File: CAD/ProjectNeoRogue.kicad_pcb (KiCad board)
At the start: 4 copper layers, 89 x 99 mm, 72 parts, among them J1 5v GND, J2 Micro_SD_Card, J3 JTAG, J4 UART, J5 Reset Jumper, J6 Boot Jumper, J8 USB_C_Plug_USB2.0, SW1 SW_SPDT, SW2 Boot, SW3 Reset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

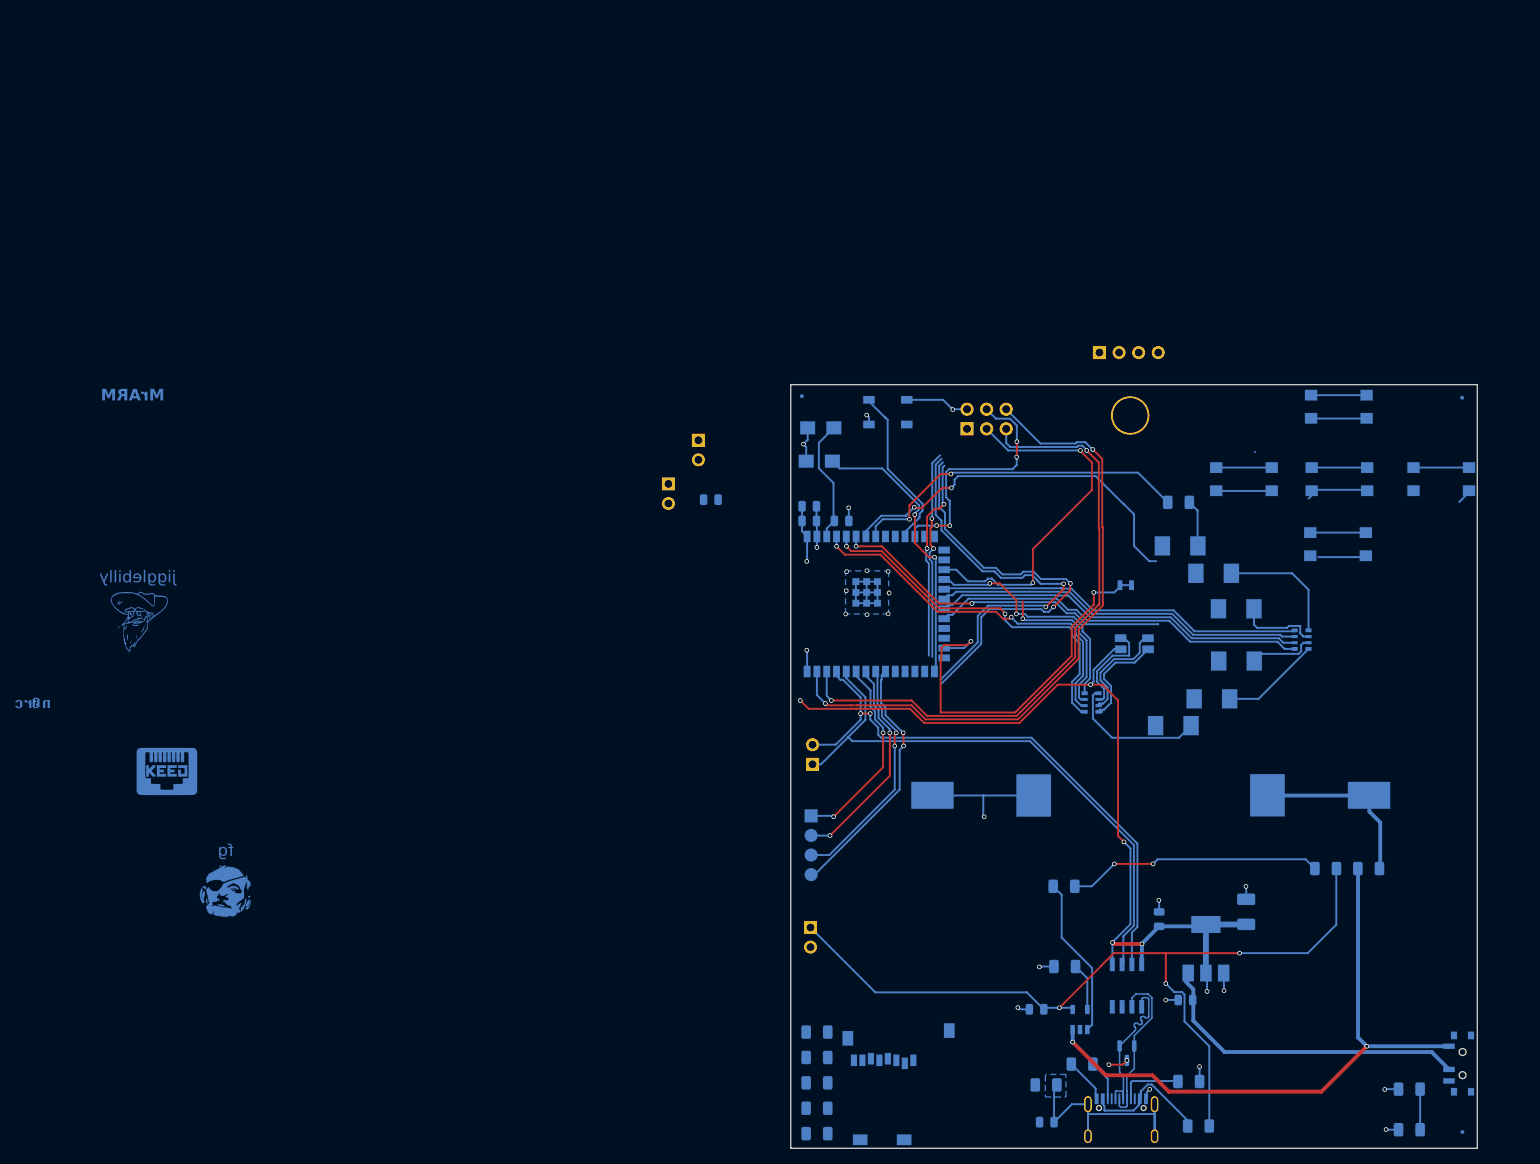
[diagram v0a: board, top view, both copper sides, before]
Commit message: adding footprints and starting to route
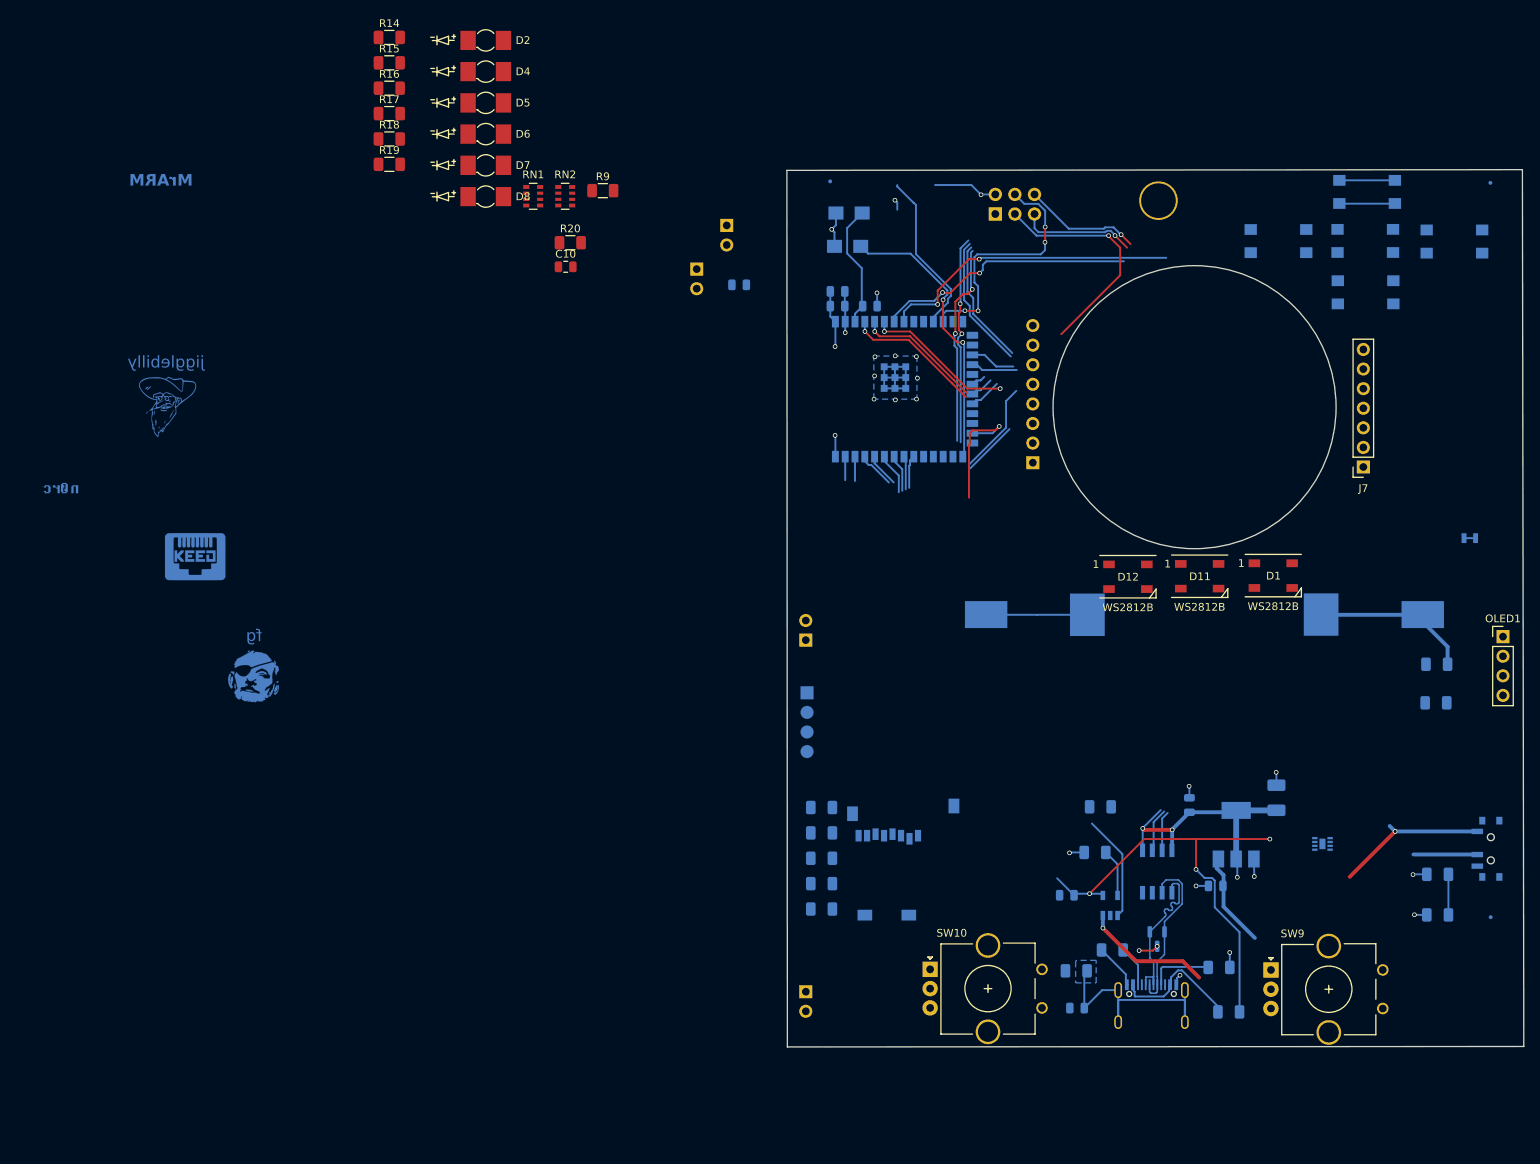
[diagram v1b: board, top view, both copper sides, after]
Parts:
- removed D3: LED, BadgePirates:LED_Osram_Lx_P47F_D2mm_ReverseMount_Proper_Mask Only
- added C10: 0.1uF, BadgePirates:C_0805_2012Metric, F.Cu at (100.4, 45.2)
- added D11: WS2812B, BadgePirates:LED_WS2812B_PLCC4_5.0x5.0mm_P3.2mm, F.Cu at (182.6, 85.3)
- added D12: WS2812B, BadgePirates:LED_WS2812B_PLCC4_5.0x5.0mm_P3.2mm, F.Cu at (173.2, 85.4)
- added J7: RoundDisplay_SPI, Connector_PinSocket_2.54mm:PinSocket_1x07_P2.54mm_Vertical, F.Cu at (203.8, 71.2)
- added J9: RoundDisplay_SPI_v2, Connector_PinSocket_2.54mm:PinSocket_1x08_P2.54mm_Vertical, B.Cu at (160.9, 70.6)
- added R14: 10k, BadgePirates:R_1206_3216Metric, F.Cu at (77.5, 15.5)
- added R15: 10k, BadgePirates:R_1206_3216Metric, F.Cu at (77.5, 18.8)
- added R16: 10k, BadgePirates:R_1206_3216Metric, F.Cu at (77.5, 22.1)
- added R17: 10k, BadgePirates:R_1206_3216Metric, F.Cu at (77.5, 25.4)
- added R18: 10k, BadgePirates:R_1206_3216Metric, F.Cu at (77.5, 28.7)
- added R19: 10k, BadgePirates:R_1206_3216Metric, F.Cu at (77.5, 31.9)
- added R20: 10K, BadgePirates:R_1206_3216Metric, F.Cu at (101.0, 42.1)
- added SW10: RotaryEncoder_Switch, Rotary_Encoder:RotaryEncoder_Alps_EC11E_Vertical_H20mm_CircularMountingHoles, F.Cu at (147.6, 136.3)
- added SW9: RotaryEncoder_Switch, Rotary_Encoder:RotaryEncoder_Alps_EC11E_Vertical_H20mm_CircularMountingHoles, F.Cu at (191.8, 136.4)
- added U5: MAX17048, BadgePirates:MAX17048_TDFN, B.Cu at (198.5, 120.0)
- D1, D4, D5, D6, D7, D8, OLED1, R9, RN1, RN2: moved to F.Cu
- D2: footprint BadgePirates:LED_RGB_1210 -> BadgePirates:LED_Osram_Lx_P47F_D2mm_ReverseMount_Proper_Mask Only; moved to F.Cu
- moved D4 124.4 mm to (90.0, 19.9)
- moved D5 121.3 mm to (90.0, 24.0)
- moved D6 115.1 mm to (90.0, 28.0)
- moved D2 114.8 mm to (90.0, 15.9)
- moved RN2 111.4 mm to (100.3, 36.1), turned to 0 degrees
- moved D7 108.2 mm to (90.0, 32.1)
- moved D8 100.8 mm to (90.0, 36.1)
- moved RN1 97.7 mm to (96.2, 36.1), turned to 0 degrees
- moved R9 84.9 mm to (105.2, 35.4)
- moved OLED1 64.0 mm to (221.9, 93.2), turned to 0 degrees
- moved D1 54.3 mm to (192.1, 85.3), turned to 0 degrees
- moved JP1 45.0 mm to (217.8, 80.4)
- moved SW7 32.8 mm to (204.1, 48.5)
- moved SW6 31.2 mm to (192.8, 41.9)
- moved SW5 31.1 mm to (204.0, 41.9)
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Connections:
- D1 pad 2: unconnected-(D1-DOUT-Pad2) -> Net-(D1-DOUT)
- D2 pad 1: Net-(D2-RK) -> GND
- D2 pad 2: VCC -> Net-(D2-A)
- RN1 pad 1: Net-(D3-A) -> Net-(D2-A)
- RN1 pad 2: Net-(D2-BK) -> unconnected-(RN1-R2.1-Pad2)
- RN1 pad 3: Net-(D2-GK) -> unconnected-(RN1-R3.1-Pad3)
- RN1 pad 4: Net-(D2-RK) -> unconnected-(RN1-R4.1-Pad4)
- RN1 pad 5: IO05 -> unconnected-(RN1-R4.2-Pad5)
- RN1 pad 6: IO04 -> unconnected-(RN1-R3.2-Pad6)
- RN1 pad 7: IO25 -> unconnected-(RN1-R2.2-Pad7)
- RN2 pad 1: Net-(D7-A) -> Net-(D4-A)
- RN2 pad 2: Net-(D6-A) -> Net-(D5-A)
- RN2 pad 3: Net-(D5-A) -> Net-(D6-A)
- RN2 pad 4: Net-(D4-A) -> Net-(D7-A)
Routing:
- net VCC: track 133.3 -> 51.6 mm, vias 9 -> 6
- net IO01: track 84.5 -> 18.6 mm, vias 2 -> 1
- net USB_TX_ESP_RX: track 75.5 -> 10.0 mm
- net USB_RX_ESP_TX: track 75.2 -> 10.00 mm, vias 2 -> 0
- net IO02: track 81.4 -> 18.2 mm, vias 2 -> 1
- net VBUS: track 111.6 -> 58.7 mm
- net IO11: track 47.9 -> 0.18 mm
- net IO12: track 48.2 -> 1.92 mm
- net IO13: track 48.7 -> 3.08 mm
- net IO14: track 49.2 -> 4.24 mm
- net Net-(SW1-A): track 79.0 -> 36.7 mm
- net IO48: track 50.0 -> 16.4 mm, vias 2 -> 1
- net GND: track 110.8 -> 77.6 mm, vias 25 -> 23
- net Net-(D10-K): track 33.1 -> 0.00 mm, vias 2 -> 0
- net IO05: track 47.9 -> 16.6 mm, vias 2 -> 1
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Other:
- board size 89 x 99 mm -> 95.5 x 113.7 mm
- board text removed: "Max17048"

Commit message: placing parts
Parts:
- C10, D2, D4, D5, D6, D7, D8, R14, R15, R16, R17, R18, R19, R20, R9, RN1, RN2: moved to B.Cu
- moved D2 132.4 mm to (217.2, 52.8), turned to 180 degrees
- moved D4 132.4 mm to (217.2, 56.9), turned to 180 degrees
- moved D5 132.4 mm to (217.2, 60.9), turned to 180 degrees
- moved D6 132.4 mm to (217.2, 65.0), turned to 180 degrees
- moved D7 132.4 mm to (217.2, 69.0), turned to 180 degrees
- moved D8 132.4 mm to (217.2, 73.1), turned to 180 degrees
- moved RN1 95.7 mm to (164.1, 103.5), turned to 180 degrees
- moved R16 94.3 mm to (140.2, 92.4), turned to 180 degrees
- moved R18 94.3 mm to (140.2, 99.0), turned to 180 degrees
- moved R14 94.3 mm to (140.2, 85.8), turned to 180 degrees
- moved R15 94.3 mm to (140.2, 89.1), turned to 180 degrees
- moved R17 94.3 mm to (140.2, 95.7), turned to 180 degrees
- moved R19 94.3 mm to (140.2, 102.3), turned to 180 degrees
- moved RN2 90.0 mm to (159.9, 103.5), turned to 180 degrees
- moved C10 89.9 mm to (159.9, 112.6), turned to 180 degrees
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
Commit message: Update ProjectNeoRogue.kicad_pcb
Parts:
- removed kibuzzard-64E63238: G***, kibuzzard-64E63238
- moved G*** 168.1 mm to (68.6, 140.2)
- moved G*** 165.4 mm to (71.0, 131.8)
- moved G*** 93.0 mm to (102.7, 138.4)
- moved REF** 73.2 mm to (87.5, 124.5)
- moved G*** 61.2 mm to (87.3, 132.8)
- moved G*** 47.3 mm to (98.8, 125.0)
- moved C1 20.3 mm to (142.6, 52.1)
- moved R7 14.5 mm to (160.3, 149.6)
- moved U1 14.5 mm to (164.7, 141.2)
- moved J1 14.5 mm to (125.3, 152.3)
- moved G*** 14.5 mm to (201.6, 142.1)
- moved J8 14.5 mm to (170.1, 152.1)
- moved R10 14.5 mm to (178.8, 149.2)
- moved R12 14.5 mm to (127.3, 138.3)
- moved R13 14.5 mm to (127.3, 141.6)
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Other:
- board text removed: "Assembled in KC by:"

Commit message: Added Tag Connect for JTAG
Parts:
- added BT2: Battery, BadgePirates:Battery - 14500, B.Cu at (355.3, -56.7)
- added C11: 100pF, Capacitor_SMD:C_0603_1608Metric_Pad1.08x0.95mm_HandSolder, B.Cu at (379.1, -42.0)
- added D3: Charging, BadgePirates:LED_1206, B.Cu at (384.0, -46.9)
- added F2: Fuse, BadgePirates:R_1206_3216Metric, B.Cu at (378.4, -47.0)
- added R21: 75, Resistor_SMD:R_0603_1608Metric_Pad0.98x0.95mm_HandSolder, B.Cu at (379.1, -39.5)
- added R22: 10K, BadgePirates:R_1206_3216Metric, B.Cu at (384.1, -41.6)
- added R24: 22, BadgePirates:R_1206_3216Metric, B.Cu at (384.1, -38.3)
- added R25: 1k, BadgePirates:R_1206_3216Metric, B.Cu at (372.1, -41.6)
- J2: footprint BadgePirates:SF-MICRO-SD -> Connector_Card:microSD_HC_Molex_104031-0811
- J3: footprint Connector_PinHeader_2.54mm:PinHeader_1x04_P2.54mm_Vertical -> Connector:Tag-Connect_TC2030-IDC-FP_2x03_P1.27mm_Vertical
- moved J3 16.9 mm to (142.3, 112.9)
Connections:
- net /BATTERY+ renamed /Power/BATTERY+
- net /Max17048/~{ALRT} renamed /Power/BATT_LVL_~{ALERT}
- J3 pad 1: TMS -> VCC
- J3 pad 2: TDI -> TMS
- J3 pad 3: TDO -> RESET
- R3 pad 1: Net-(D10-K) -> Net-(D3-K)
- U5 pad 7: IO09 -> /Power/BATT_LVL_SCL
- U5 pad 8: IO08 -> /Power/BATT_LVL_SDA

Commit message: Layout progress
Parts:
- removed D10: Charging, BadgePirates:LED_1206
- removed Fid3, Fid_2: Fiducial, Fiducial:Fiducial_0.5mm_Mask1mm
- removed Fid_1: fid, Fiducial:Fiducial_0.5mm_Mask1mm
- removed the G*** at (68.6, 140.2)
- removed the G*** at (71.0, 131.8)
- removed the REF** at (171.0, 49.8)
- removed RN1: 1k_Array, BadgePirates:R_Array_Convex_4x0603
- SW10, SW9: footprint Rotary_Encoder:RotaryEncoder_Alps_EC11E_Vertical_H20mm_CircularMountingHoles -> Rotary_Encoder:RotaryEncoder_Alps_EC11E-Switch_Vertical_H20mm_CircularMountingHoles
- moved R24 277.8 mm to (138.6, 91.8)
- moved R22 277.7 mm to (138.6, 88.2)
- moved C11 269.8 mm to (143.1, 88.9)
- moved R21 267.3 mm to (143.1, 86.1), turned to 0 degrees
- moved D3 262.7 mm to (193.0, 133.5)
- moved BT2 250.4 mm to (177.0, 119.2)
- moved F2 233.7 mm to (206.3, 111.1), turned to -90 degrees
- moved R25 194.9 mm to (207.3, 62.5), turned to 0 degrees
- moved R4 68.7 mm to (133.9, 60.1)
- moved JP1 58.7 mm to (153.0, 90.2)
- moved RN2 56.4 mm to (203.4, 90.0), turned to -90 degrees
- moved C10 52.0 mm to (204.8, 135.0), turned to 0 degrees
- moved R20 49.2 mm to (201.5, 131.3), turned to 0 degrees
- moved R9 47.8 mm to (203.8, 94.0)
- moved R3 34.5 mm to (197.1, 136.1), turned to -90 degrees
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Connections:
- BT1 pad 1: /Power/BATTERY+ -> /Power/BATTERY1+
- BT2 pad 1: Net-(BT2-+) -> /Power/BATTERY2+
- D19 pad 1: D+ -> D-
- D19 pad 2: D- -> D+
- F1 pad 1: /Power/BATTERY+ -> /Power/BATTERY2+
- F2 pad 1: /Power/BATTERY+ -> /Power/BATTERY1+
- F2 pad 2: Net-(BT2-+) -> /Power/BATTERY2+
- U5 pad 7: /Power/BATT_LVL_SCL -> IO09
- U5 pad 8: /Power/BATT_LVL_SDA -> IO08
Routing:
- net IO08: track 32.3 -> 103.3 mm, vias 4 -> 2
- net GND: track 77.6 -> 10.1 mm, vias 23 -> 20
- net IO09: track 35.8 -> 98.9 mm, vias 1 -> 2
- net VCC: track 51.6 -> 7.89 mm, vias 6 -> 10
- net Boot: track 37.0 -> 0.00 mm, vias 2 -> 0
- net SCL: track 33.9 -> 0.00 mm, vias 2 -> 0
- net Net-(J8-SHIELD): track 33.0 -> 0.00 mm
- net VBUS: track 58.7 -> 89.7 mm, vias 3 -> 2
- net IO20: track 29.6 -> 0.00 mm
- net IO37: track 27.8 -> 0.00 mm, vias 2 -> 0
- net IO38: track 26.2 -> 0.00 mm, vias 2 -> 0
- net +BATT: track 20.7 -> 44.8 mm
- net IO36: track 23.5 -> 0.00 mm
- net /Power/BATTERY+: track 22.6 -> 0.00 mm
- net Net-(D4-A): track 0.00 -> 21.8 mm
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- added copper zone on B.Cu, net /Power/BATTERY1+
- added copper zone on F.Cu, net /Power/BATTERY1+
- added copper zone on In1.Cu, net GND
- added copper zone on B.Cu, net VCC
- added copper zone on In2.Cu, net VCC
- removed copper zone on In2.Cu, net GND
- removed copper zone on B.Cu, net Net-(J8-SHIELD)
- removed copper zone on In1.Cu, net VCC
